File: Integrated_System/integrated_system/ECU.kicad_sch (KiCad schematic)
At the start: 24 parts, among them J1 Jack-DC, J2 Fan 1, J3 Fan 2, J4 Fan 3, Q2 TN0702N3, Q3 TN0702N3, Q4 TN0702N3, U1 DC to DC Buck Converter 12V t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, U5 SGP30, U6 BME280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

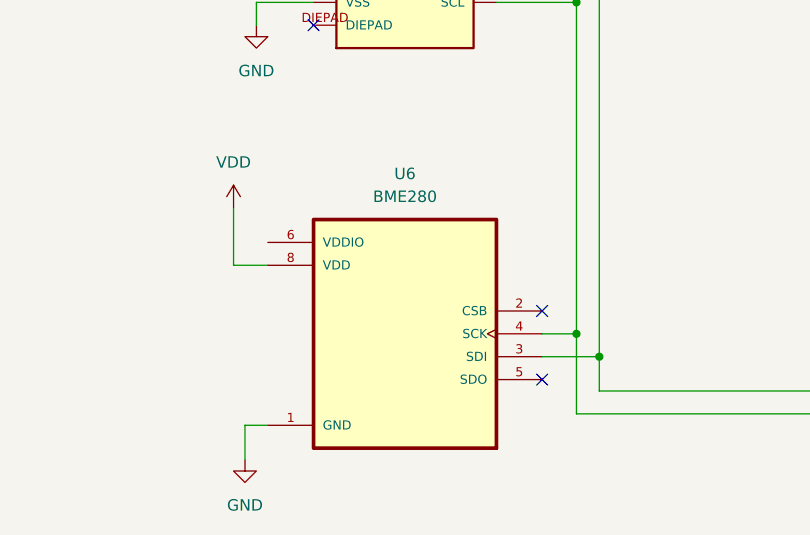
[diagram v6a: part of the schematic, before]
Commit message: Replaced with bme680 sensor
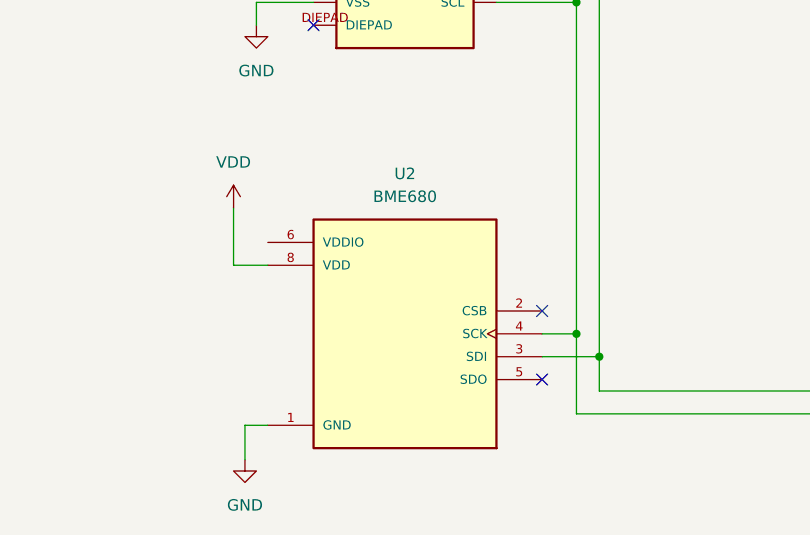
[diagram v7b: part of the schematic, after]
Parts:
- removed U6: BME280, BME280:PSON65P250X250X100-8N, symbol BME280:BME280
- added U2: BME680, BME680:PSON80P300X300X100-8N, symbol BME680:BME680
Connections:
- net GND: now also U2.1 (GND), U2.7 (GND)
- net VDD: now also U2.8 (VDD)
- net at A1.18 (SCL/IO22), U5.6 (SCL), U7.3 (TX/SCL): now also U2.4 (SCK)
- net at A1.17 (SDA/IO23), U5.3 (SDA), U7.4 (RX/SDA): now also U2.3 (SDI)
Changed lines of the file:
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@@
-	)
-	(symbol
-		(lib_id "BME280:BME280")
-		(at 60.96 167.64 0)
-		(mirror y)
-		(unit 1)
-		(exclude_from_sim no)
-		(in_bom yes)
-		(on_board yes)
-		(dnp no)
-		(fields_autoplaced yes)
-		(property "Reference" "U6"
-			(at 60.96 149.86 0)
-			(effects
-				(font
-					(size 1.27 1.27)
-				)
-			)
-		)
-		(property "Value" "BME280"
-			(at 60.96 152.4 0)
-			(effects
-				(font
-					(size 1.27 1.27)
-				)
-			)
-		)
-		(property "Footprint" "BME280:PSON65P250X250X100-8N"
-			(at 60.96 167.64 0)
-			(effects
-				(font
-					(size 1.27 1.27)
-				)
-				(justify bottom)
-				(hide yes)
-			)
-		)
-		(property "Datasheet" ""
-			(at 60.96 167.64 0)
-			(effects
-				(font
-					(size 1.27 1.27)
-				)
-				(hide yes)
-			)
-		)
-		(property "Description" ""
-			(at 60.96 167.64 0)
-			(effects
-				(font
-					(size 1.27 1.27)
-				)
-				(hide yes)
-			)
-		)
-		(property "MF" "Bosch"
-			(at 60.96 167.64 0)
-			(effects
-				(font
-					(size 1.27 1.27)
-				)
-				(justify bottom)
-				(hide yes)
-			)
-		)
-		(property "DESCRIPTION" "Integrated pressure, humidity and temperature sensor; 8-pin 2.5x2.5x0.93mm LGA"
-			(at 60.96 167.64 0)
-			(effects
-				(font
-					(size 1.27 1.27)
-				)
-				(justify bottom)
-				(hide yes)
-			)
-		)
-		(property "PACKAGE" "LGA-8 Bosch"
-			(at 60.96 167.64 0)
-			(effects
-				(font
-					(size 1.27 1.27)
-				)
-				(justify bottom)
-				(hide yes)
-			)
-		)
-		(property "PRICE" "4.94 USD"
-			(at 60.96 167.64 0)
-			(effects
-				(font
-					(size 1.27 1.27)
-				)
-				(justify bottom)
-				(hide yes)
-			)
-		)
-		(property "Package" "LGA-8 Bosch"
-			(at 60.96 167.64 0)
-			(effects
-				(font
-					(size 1.27 1.27)
-				)
-				(justify bottom)
-				(hide yes)
-			)
-		)
-		(property "Check_prices" "https://www.snapeda.com/parts/BME280/Bosch/view-part/?ref=eda"
-			(at 60.96 167.64 0)
-			(effects
-				(font
-					(size 1.27 1.27)
-				)
-				(justify bottom)
-				(hide yes)
-			)
-		)
-		(property "STANDARD" "IPC-7351B"
-			(at 60.96 167.64 0)
-			(effects
-				(font
-					(size 1.27 1.27)
-				)
-				(justify bottom)
-				(hide yes)
-			)
-		)
-		(property "SnapEDA_Link" "https://www.snapeda.com/parts/BME280/Bosch/view-part/?ref=snap"
-			(at 60.96 167.64 0)
-			(effects
-				(font
-					(size 1.27 1.27)
-				)
-				(justify bottom)
-				(hide yes)
-			)
-		)
-		(property "MP" "BME280"
-			(at 60.96 167.64 0)
-			(effects
-				(font
-					(size 1.27 1.27)
-				)
-				(justify bottom)
-				(hide yes)
-			)
-		)
-		(property "Purchase-URL" "https://www.snapeda.com/api/url_track_click_mouser/?unipart_id=49769&manufacturer=Bosch&part_name=BME280&search_term=None"
-			(at 60.96 167.64 0)
-			(effects
-				(font
-					(size 1.27 1.27)
-				)
-				(justify bottom)
-				(hide yes)
-			)
-		)
-		(property "Price" "None"
-			(at 60.96 167.64 0)
-			(effects
-				(font
-					(size 1.27 1.27)
-				)
-				(justify bottom)
-				(hide yes)
-			)
-		)
-		(property "Availability" "In Stock"
-			(at 60.96 167.64 0)
-			(effects
-				(font
-					(size 1.27 1.27)
-				)
-				(justify bottom)
-				(hide yes)
-			)
-		)
-		(property "AVAILABILITY" "Good"
-			(at 60.96 167.64 0)
-			(effects
-				(font
-					(size 1.27 1.27)
-				)
-				(justify bottom)
-				(hide yes)
-			)
-		)
-		(property "Description_1" "Board Mount Humidity Sensors MEMS humidity, pressure and temperature sensor"
-			(at 60.96 167.64 0)
-			(effects
-				(font
-					(size 1.27 1.27)
-				)
-				(justify bottom)
-				(hide yes)
-			)
-		)
-		(pin "8"
-		)
-		(pin "2"
-		)
-		(pin "7"
-		)
-		(pin "6"
-		)
-		(pin "4"
-		)
-		(pin "1"
-		)
-		(pin "3"
-		)
-		(pin "5"
-		)
-		(instances
-			(project ""
-				(path "/e09e0073-4b34-4087-926d-a963f587ec36/d64a58e5-7375-438d-b343-064b897cc797"
-					(reference "U6")
-					(unit 1)
-				)
-			)
-		)
 	)
 	(symbol
@@
 					(unit 1)
 				)
+			)
+		)
+	)
+	(symbol
+		(lib_id "BME680:BME680")
+		(at 60.96 167.64 0)
+		(mirror y)
+		(unit 1)
+		(exclude_from_sim no)
+		(in_bom yes)
+		(on_board yes)
+		(dnp no)
+		(fields_autoplaced yes)
+		(property "Reference" "U2"
+			(at 60.96 149.86 0)
+			(effects
+				(font
+					(size 1.27 1.27)
+				)
+			)
+		)
+		(property "Value" "BME680"
+			(at 60.96 152.4 0)
+			(effects
+				(font
+					(size 1.27 1.27)
+				)
+			)
+		)
+		(property "Footprint" "BME680:PSON80P300X300X100-8N"
+			(at 60.96 167.64 0)
+			(effects
+				(font
+					(size 1.27 1.27)
+				)
+				(justify bottom)
+				(hide yes)
+			)
+		)
+		(property "Datasheet" ""
+			(at 60.96 167.64 0)
+			(effects
+				(font
+					(size 1.27 1.27)
+				)
+				(hide yes)
+			)
+		)
+		(property "Description" ""
+			(at 60.96 167.64 0)
+			(effects
+				(font
+					(size 1.27 1.27)
+				)
+				(hide yes)
+			)
+		)
+		(property "MF" "Bosch Sensortec"
+			(at 60.96 167.64 0)
+			(effects
+				(font
+					(size 1.27 1.27)
+				)
+				(justify bottom)
+				(hide yes)
+			)
+		)
+		(property "SNAPEDA_PACKAGE_ID" "21135"
+			(at 60.96 167.64 0)
+			(effects
+				(font
+					(size 1.27 1.27)
+				)
+				(justify bottom)
+				(hide yes)
+			)
+		)
+		(property "Package" "LGA-8 Bosch Tools"
+			(at 60.96 167.64 0)
+			(effects
+				(font
+					(size 1.27 1.27)
+				)
+				(justify bottom)
+				(hide yes)
+			)
+		)
+		(property "Price" "None"
+			(at 60.96 167.64 0)
+			(effects
+				(font
+					(size 1.27 1.27)
+				)
+				(justify bottom)
+				(hide yes)
+			)
+		)
+		(property "Check_prices" "https://www.snapeda.com/parts/BME680/Bosch/view-part/?ref=eda"
+			(at 60.96 167.64 0)
+			(effects
+				(font
+					(size 1.27 1.27)
+				)
+				(justify bottom)
+				(hide yes)
+			)
+		)
+		(property "STANDARD" "Manufacturer Recommendations"
+			(at 60.96 167.64 0)
+			(effects
+				(font
+					(size 1.27 1.27)
+				)
+				(justify bottom)
+				(hide yes)
+			)
+		)
+		(property "PARTREV" "1.9"
+			(at 60.96 167.64 0)
+			(effects
+				(font
+					(size 1.27 1.27)
+				)
+				(justify bottom)
+				(hide yes)
+			)
+		)
+		(property "SnapEDA_Link" "https://www.snapeda.com/parts/BME680/Bosch/view-part/?ref=snap"
+			(at 60.96 167.64 0)
+			(effects
+				(font
+					(size 1.27 1.27)
+				)
+				(justify bottom)
+				(hide yes)
+			)
+		)
+		(property "MP" "BME680"
+			(at 60.96 167.64 0)
+			(effects
+				(font
+					(size 1.27 1.27)
+				)
+				(justify bottom)
+				(hide yes)
+			)
+		)
+		(property "Description_1" "Gas, Humidity, Pressure, Temperature Sensor I2C, SPI Output"
+			(at 60.96 167.64 0)
+			(effects
+				(font
+					(size 1.27 1.27)
+				)
+				(justify bottom)
+				(hide yes)
+			)
+		)
+		(property "MANUFACTURER" "Bosch Sensortec"
+			(at 60.96 167.64 0)
+			(effects
+				(font
+					(size 1.27 1.27)
+				)
+				(justify bottom)
+				(hide yes)
+			)
+		)
+		(property "Availability" "In Stock"
+			(at 60.96 167.64 0)
+			(effects
+				(font
+					(size 1.27 1.27)
+				)
+				(justify bottom)
+				(hide yes)
+			)
+		)
+		(property "MAXIMUM_PACKAGE_HEIGHT" "1mm"
+			(at 60.96 167.64 0)
+			(effects
+				(font
+					(size 1.27 1.27)
+				)
+				(justify bottom)
+				(hide yes)
+			)
+		)
+		(pin "7"
+		)
+		(pin "3"
+		)
+		(pin "4"
+		)
+		(pin "2"
+		)
+		(pin "8"
+		)
+		(pin "6"
+		)
+		(pin "1"
+		)
+		(pin "5"
+		)
+		(instances
+			(project ""
+				(path "/e09e0073-4b34-4087-926d-a963f587ec36/d64a58e5-7375-438d-b343-064b897cc797"
+					(reference "U2")
+					(unit 1)
+				)

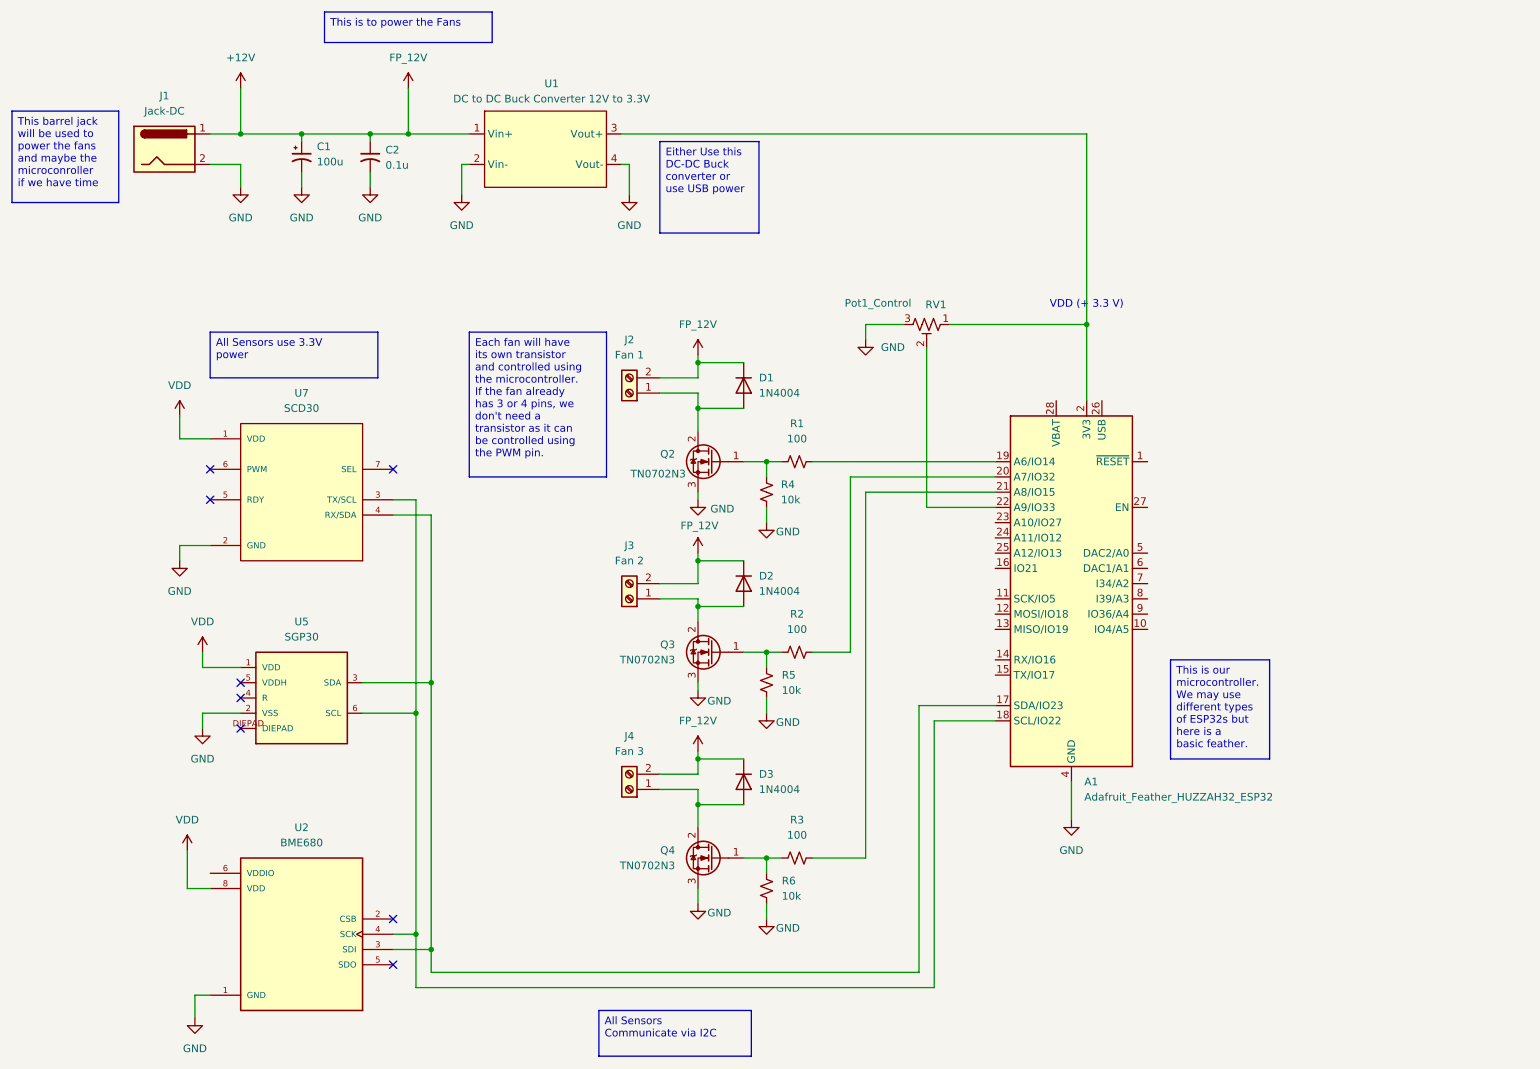
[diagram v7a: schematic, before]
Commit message: Added LEDs
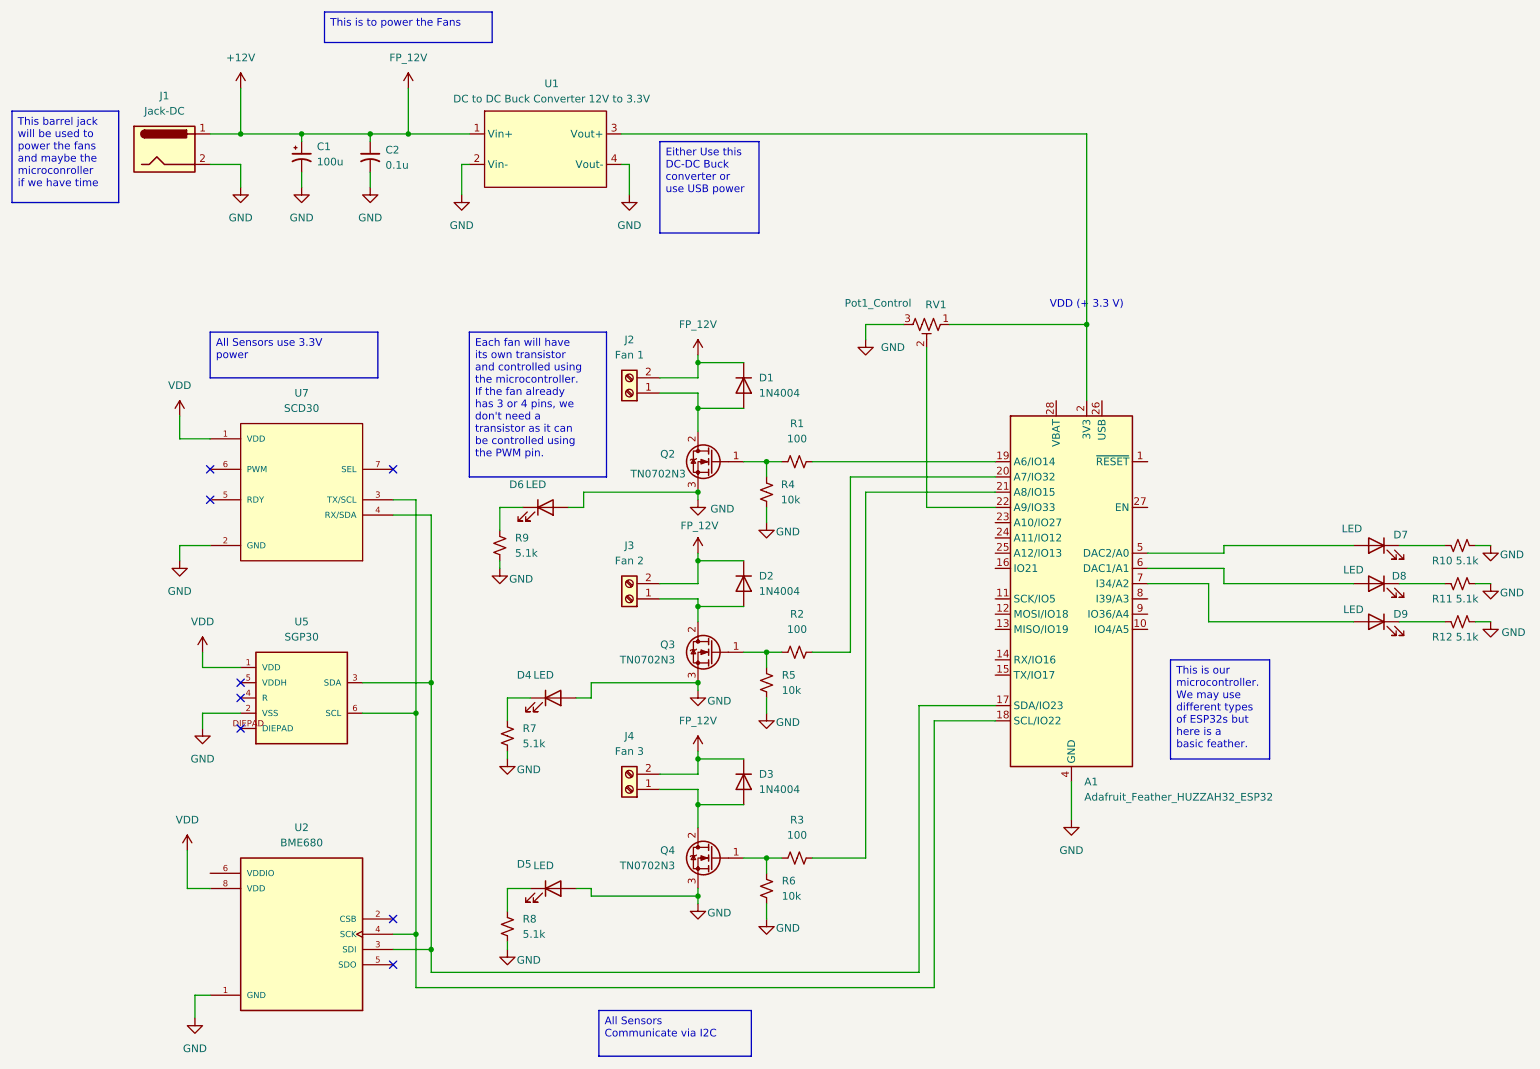
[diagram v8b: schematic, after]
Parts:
- added D4, D5, D6, D7, D8, D9: LED, symbol Device:LED
- added R10, R11, R12, R7, R8, R9: 5.1k, symbol Device:R_Small_US
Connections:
- net GND: now also D4.2 (A), D5.2 (A), D6.2 (A), R10.1, R11.1, R12.1, R7.1, R8.1, R9.1
- net at A1.5 (DAC2/A0): now also D7.2 (A)
- net at A1.6 (DAC1/A1): now also D8.2 (A)
- net at A1.7 (I34/A2): now also D9.2 (A)
- new net: D4.1 (K), R7.2
- new net: D5.1 (K), R8.2
- new net: D9.1 (K), R12.2
- new net: D6.1 (K), R9.2
- new net: D8.1 (K), R11.2
- new net: D7.1 (K), R10.2
